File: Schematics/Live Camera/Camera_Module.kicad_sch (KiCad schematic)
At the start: 87 parts, among them J1 Stack Male Edge Connector, J2 SWD_01x04_Pin, J4 USB_C_Female_USB2_Small, J6 CAM_PWR, J7 CAM_DAT, Q3 AO3400A, Q3 AO3401A, Q4 AO3400A, SW1 SW_STM_RESET, SW2 SW_STM_BOOT_MODE, U1 CP2102N-Axx-xQFN28, U1 LM66100DCKR, U1 STM32F103CBT6, U10 ACS70331EOLC, U12 AMS1117-3.3, U3 W25Q128JVS, U5 LM66100DCKR, U6 LM66100DCKR, U8 ISO1042BDWVR, Y1 X322516MMB4SI

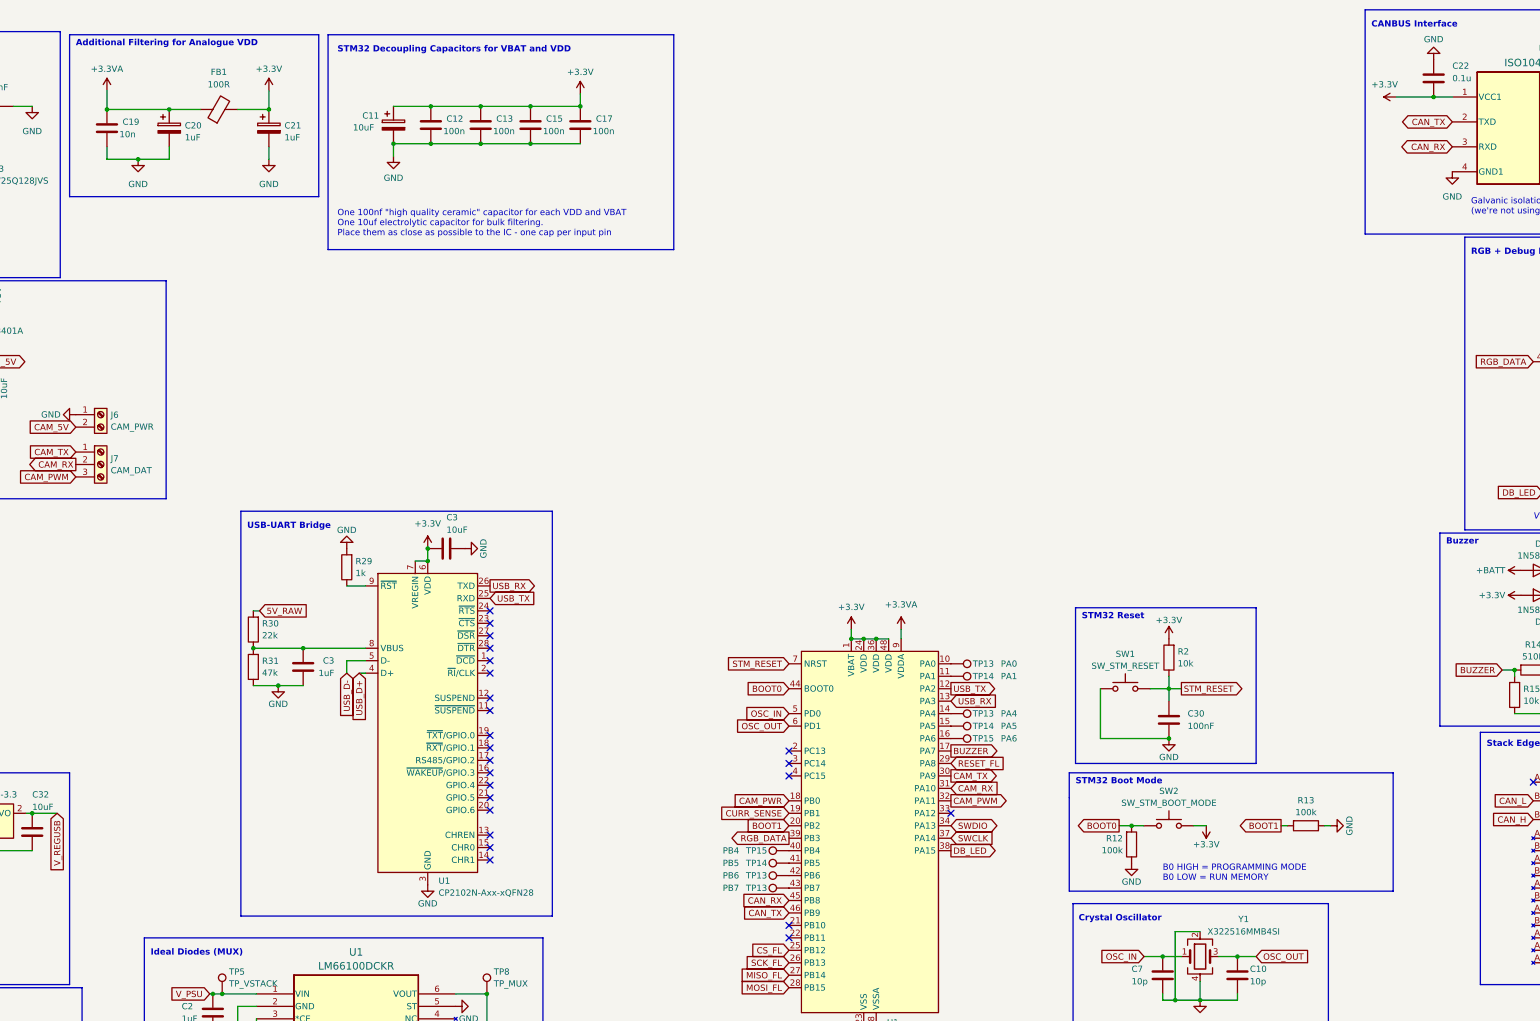
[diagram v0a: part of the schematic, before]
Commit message: Updated Live Camera Circuit
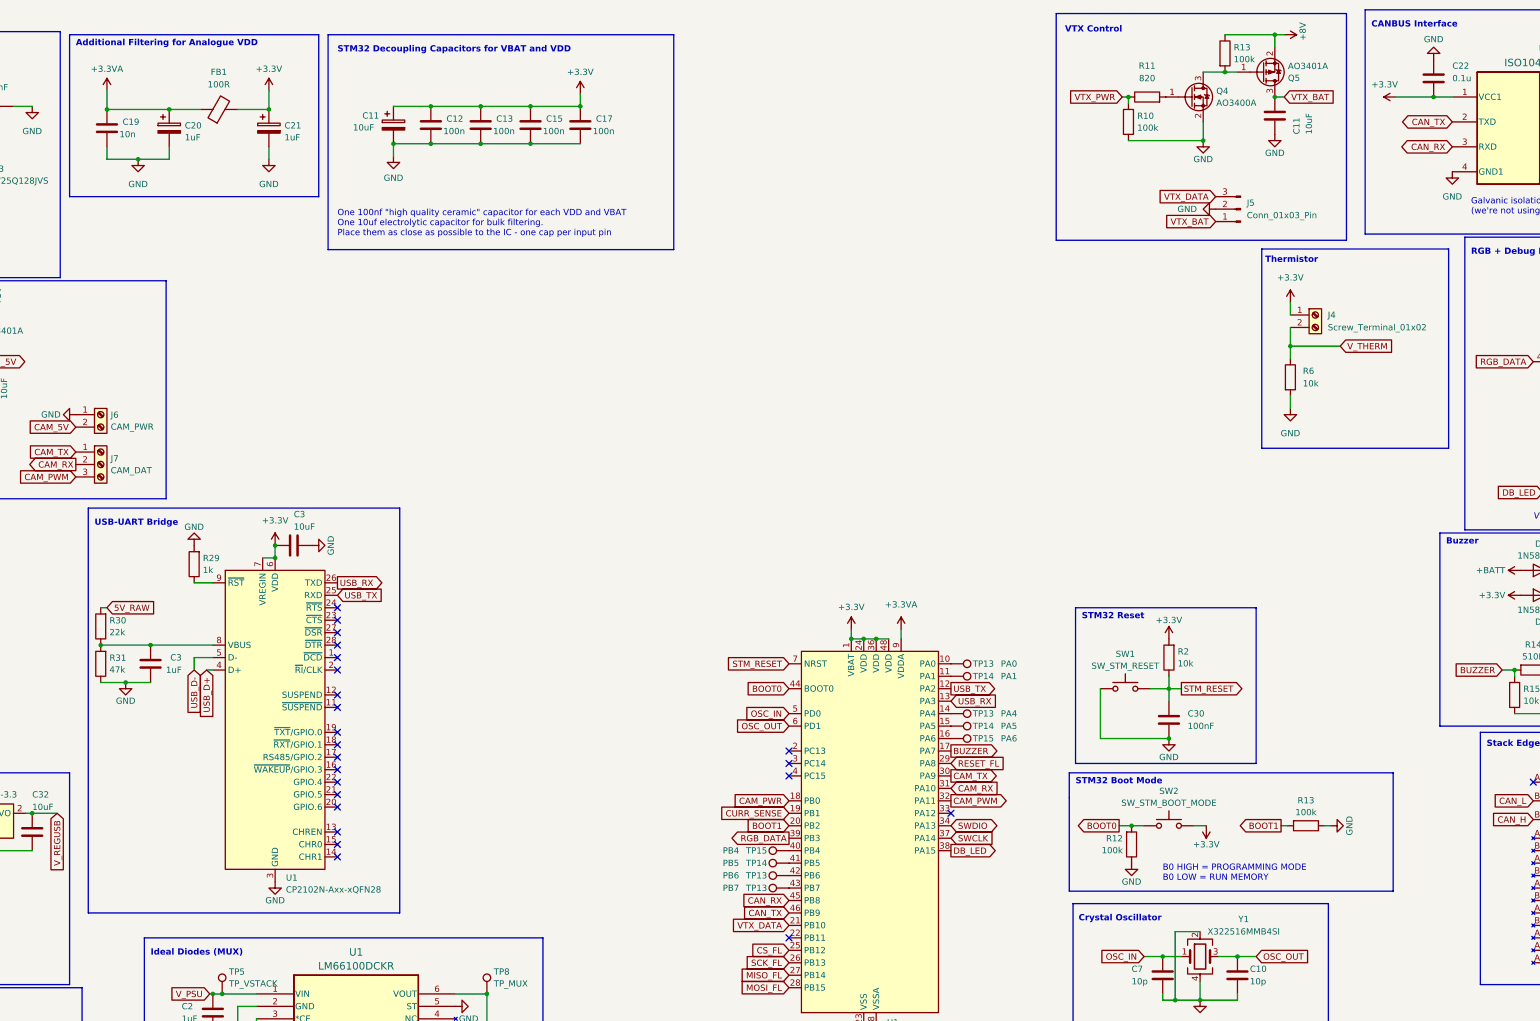
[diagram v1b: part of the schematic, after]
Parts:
- added C11: 10uF, Capacitor_SMD:C_0603_1608Metric, symbol Device:C
- added J4: Screw_Terminal_01x02, symbol Connector:Screw_Terminal_01x02
- added J5: Conn_01x03_Pin, symbol Connector:Conn_01x03_Pin
- added Q4: AO3400A, Package_TO_SOT_SMD:SOT-23, symbol Transistor_FET:AO3400A
- added Q5: AO3401A, Package_TO_SOT_SMD:SOT-23, symbol Transistor_FET:AO3401A
- added R10, R13: 100k, Resistor_SMD:R_0603_1608Metric, symbol Device:R
- added R11: 820, Resistor_SMD:R_0603_1608Metric, symbol Device:R
- added R6: 10k, symbol Device:R
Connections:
- net +3.3V: now also J4.1 (Pin_1)
- net GND: now also C11.2, J5.2 (Pin_2), Q4.2 (S), R10.2, R6.2
- net VTX_DATA: now reaches U1.21 (PB10)
- net VTX_DATA: now also J5.3 (Pin_3)
- new net: Q4.3 (D), Q5.1 (G), R13.2
- new net: Q4.1 (G), R11.2
- new net +8V: Q5.2 (S), R13.1
- new net VTX_BAT: C11.1, J5.1 (Pin_1), Q5.3 (D)
- new net VTX_PWR: R10.1, R11.1
- new net V_THERM: J4.2 (Pin_2), R6.1
- no-connect marks 32 -> 31
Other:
- note added: "Thermistor"
- note added: "VTX Control"
- moved on the sheet: C3, R29, R30, R31, U1

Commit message: Added Camera Module Layout
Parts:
- J4: footprint (none) -> TerminalBlock_TE-Connectivity:TerminalBlock_TE_282834-2_1x02_P2.54mm_Horizontal
- J5: footprint (none) -> Connector_PinHeader_1.27mm:PinHeader_1x03_P1.27mm_Horizontal
- R6: footprint (none) -> Resistor_SMD:R_0603_1608Metric
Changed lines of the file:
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@@
 			)
 		)
-		(property "Footprint" ""
+		(property "Footprint" "TerminalBlock_TE-Connectivity:TerminalBlock_TE_282834-2_1x02_P2.54mm_Horizontal"
 			(at 332.74 74.93 0)
 			(effects
@@
 			)
 		)
-		(property "Footprint" ""
+		(property "Footprint" "Resistor_SMD:R_0603_1608Metric"
 			(at 325.882 87.63 90)
 			(effects
@@
 			)
 		)
-		(property "Footprint" ""
+		(property "Footprint" "Connector_PinHeader_1.27mm:PinHeader_1x03_P1.27mm_Horizontal"
 			(at 317.5 53.34 0)
 			(effects

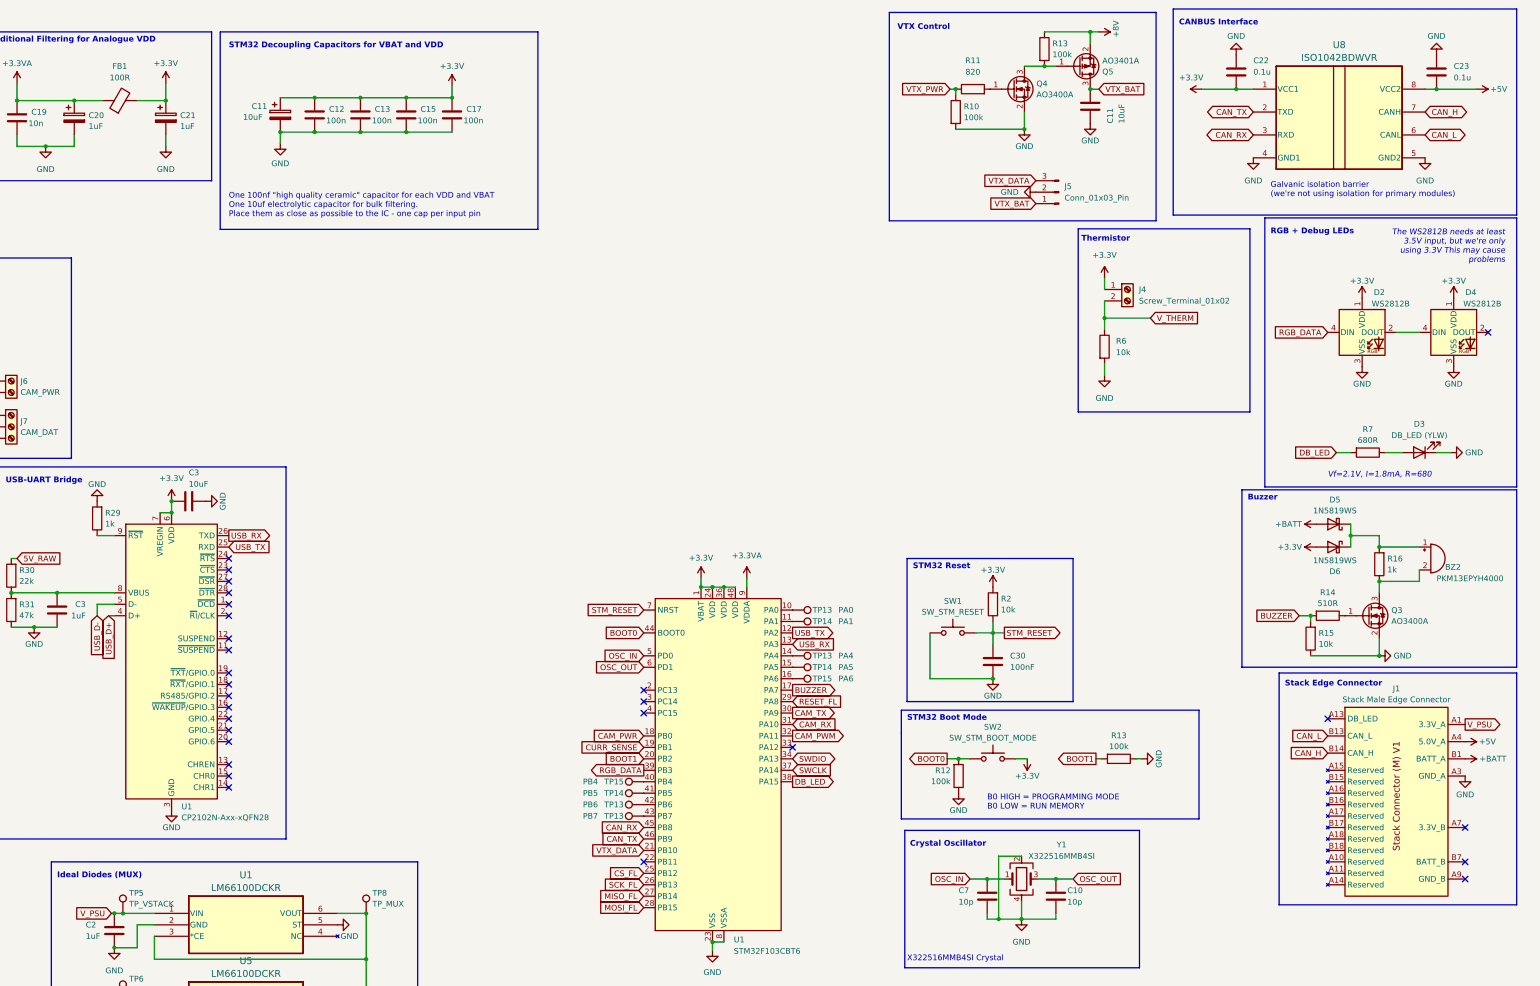
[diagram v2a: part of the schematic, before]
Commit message: Updated the Camera Module
-connect the thermistor vdiv (V_THERM) to the microcontroller (analog pin)
-add the correct battery connector for the VTX battery (Mate-n-lok, same as on power module / altimeter)
- plus an extra connector for the screw switch,
-connect the VTX control mosfet to the microcontroller
- change the CP2102's reset resistor (R25) to be a pull UP rather than a pull DOWN
-replace the 3-pin pin headers with a proper screw terminal.
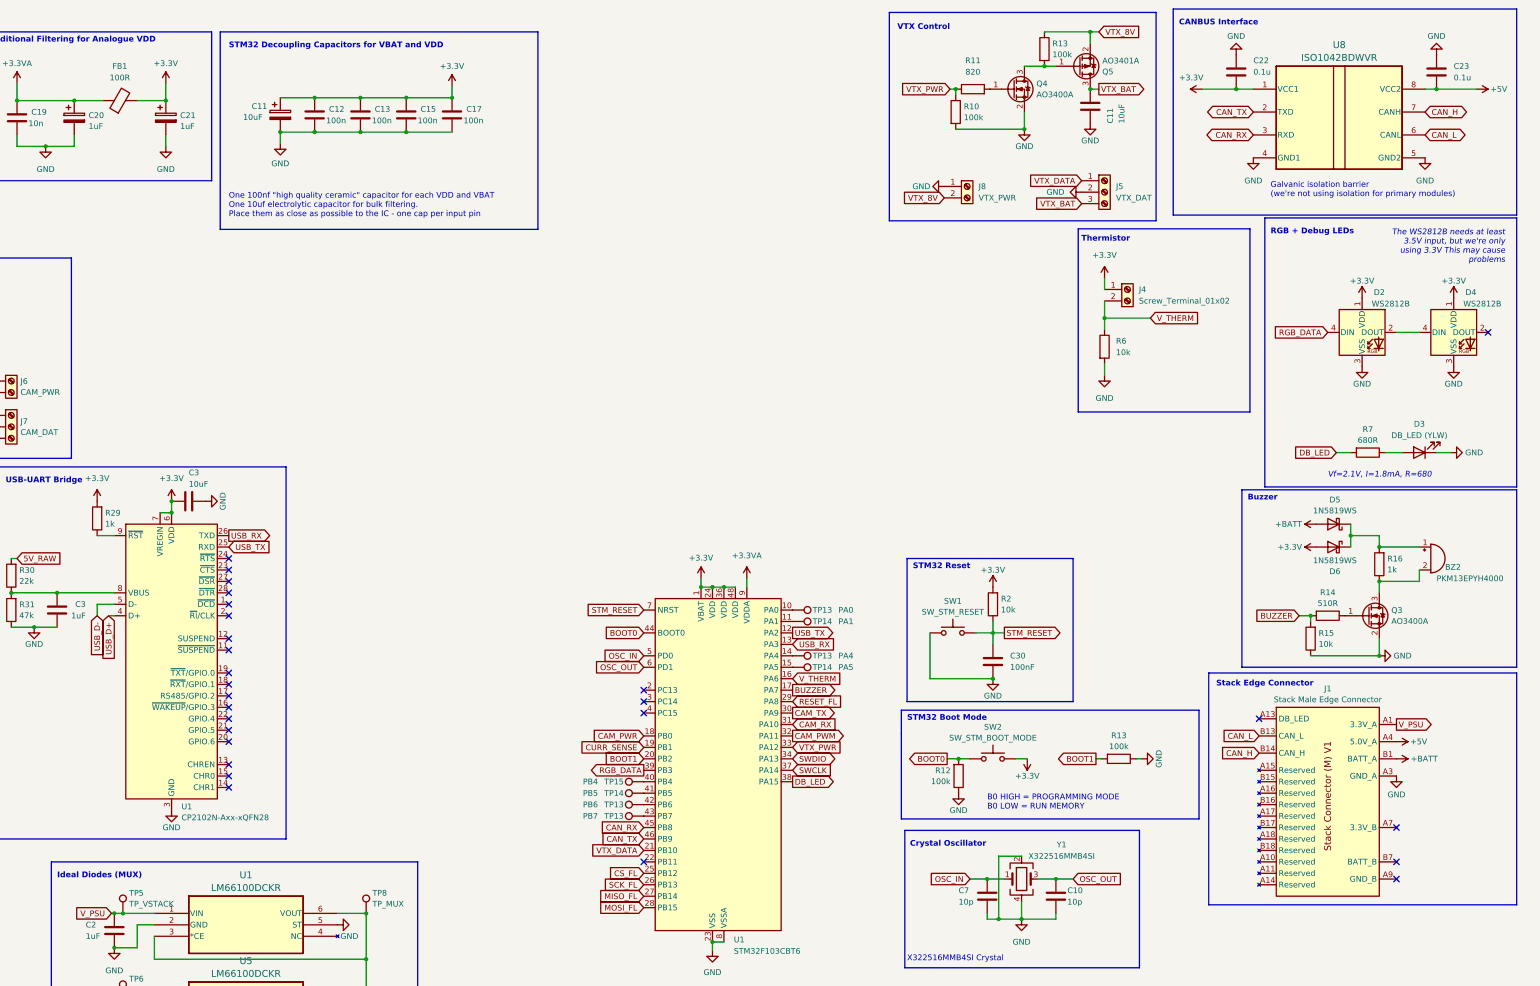
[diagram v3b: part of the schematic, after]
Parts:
- removed J5: Conn_01x03_Pin, Connector_PinHeader_1.27mm:PinHeader_1x03_P1.27mm_Horizontal, symbol Connector:Conn_01x03_Pin
- removed TP15: PA6, TestPoint:TestPoint_Pad_1.5x1.5mm, symbol Connector:TestPoint
- added J5: VTX_DAT, TerminalBlock_TE-Connectivity:TerminalBlock_TE_282834-3_1x03_P2.54mm_Horizontal, symbol Connector:Screw_Terminal_01x03
- added J8: VTX_PWR, TerminalBlock_TE-Connectivity:TerminalBlock_TE_282834-2_1x02_P2.54mm_Horizontal, symbol Connector:Screw_Terminal_01x02
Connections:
- net +3.3V: now also R29.2
- net GND: now also J5.2 (Pin_2), J8.1 (Pin_1); no longer R29.2
- net VTX_BAT: now also J5.3 (Pin_3)
- net VTX_DATA: now also J5.1 (Pin_1)
- net VTX_PWR: now also U1.33 (PA12)
- net V_THERM: now also U1.16 (PA6)
- net +8V renamed VTX_8V
- net VTX_8V: now also J8.2 (Pin_2)
- no-connect marks 31 -> 30
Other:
- moved on the sheet: J1

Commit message: Removed current sensor
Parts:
- removed C18: 0.1uF, Capacitor_SMD:C_0603_1608Metric, symbol Device:C
- removed TP2: TP_ISENSE, TestPoint:TestPoint_Pad_1.5x1.5mm, symbol Connector:TestPoint
- removed TP8: TP_MUX, TestPoint:TestPoint_Pad_1.5x1.5mm, symbol Connector:TestPoint
- removed U10: ACS70331EOLC, footprints:SOIC127P600X175-8N, symbol Sensor_Current:ACS706xLC-05C
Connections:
- net V_MUX is gone; now on net +3.3V: C14.1, U1.3 (*CE), U1.6 (VOUT), U5.3 (*CE), U5.6 (VOUT), U6.3 (*CE), U6.6 (VOUT)
- net CURR_SENSE: no longer names the net of U1.19 (PB1)
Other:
- note added: "3.3V Output"
- note added: "Vf=2.8V, R=0.15mA, R=3.3k"
- note removed: "Current Sense & 3.3V Output"
- note removed: "Vf=2.9V, I=????mA, R=3.3k"
- note removed: "decoupling cap; place close to ACS70331"
- title: QRET 23-24 SRAD Sensors Module (COTIJA) -> QRET 24-25 SRAD Camera Module (????)
- moved on the sheet: BZ2, C11, C14, C2, C3, C31, C32, C4, C6, D1, D5, D6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
